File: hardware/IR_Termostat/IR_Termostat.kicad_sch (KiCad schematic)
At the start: 42 parts, among them J1 USB_C_Receptacle_PowerOnly_6P, J2 JST-PH-2mm, J3 Conn_01x03_Pin, Q1 PMOS, SW1 SW_Push_Dual, U1 TP4056-42-ESOP8, U2 XC6206P-3.3V, U4 MLX90614ESF-BAA-000-TU, U5 CH32V003JxMx, U6 DM-OLED096-636

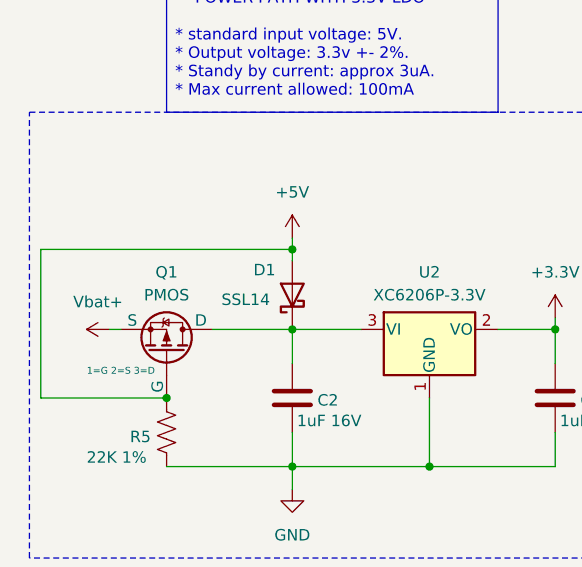
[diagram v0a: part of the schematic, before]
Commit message: Fix: power path mosfet footprint
 The footprint of the power path mosfet now it's pin-to-pin with the skemathic.
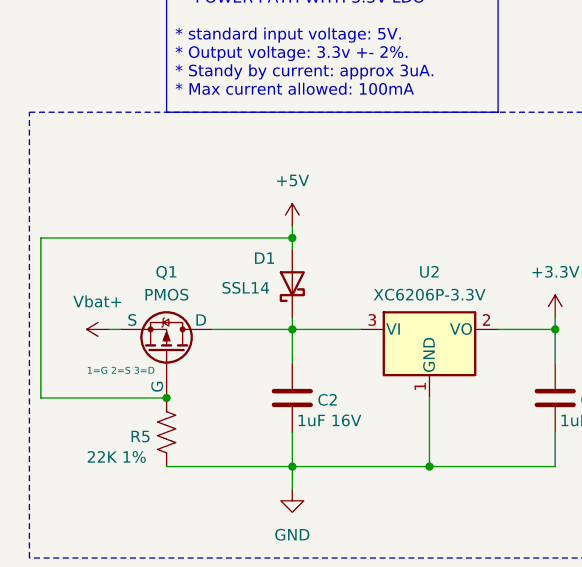
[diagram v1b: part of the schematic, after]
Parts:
- U4: footprint MLX90614ESF-BAA-000-TU:TO254P942H425-4 -> Library:TO254P942H425-4
- U6: footprint DM-OLED096-636:MODULE_DM-OLED096-636 -> Library:MODULE_DM-OLED096-636
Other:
- moved on the sheet: D1
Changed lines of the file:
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@@
 	)
 	(junction
+		(at 44.45 120.65)
+		(diameter 0)
+		(color 0 0 0 0)
+	)
+	(junction
 		(at 134.62 53.34)
 		(diameter 0)
@@
 	)
 	(junction
-		(at 44.45 121.92)
-		(diameter 0)
-		(color 0 0 0 0)
-	)
-	(junction
 		(at 148.59 53.34)
 		(diameter 0)
@@
 	(wire
 		(pts
-			(xy 44.45 120.65) (xy 44.45 121.92)
+			(xy 44.45 119.38) (xy 44.45 120.65)
 		)
 		(stroke
@@
 	(wire
 		(pts
-			(xy 16.51 121.92) (xy 16.51 138.43)
+			(xy 16.51 120.65) (xy 16.51 138.43)
 		)
 		(stroke
@@
 	(wire
 		(pts
+			(xy 44.45 129.54) (xy 44.45 130.81)
+		)
+		(stroke
+			(width 0)
+			(type default)
+		)
+	)
+	(wire
+		(pts
 			(xy 165.1 62.6446) (xy 165.1 69.85)
 		)
@@
 	(wire
 		(pts
-			(xy 44.45 121.92) (xy 44.45 123.19)
-		)
-		(stroke
-			(width 0)
-			(type default)
-		)
-	)
-	(wire
-		(pts
 			(xy 173.99 55.88) (xy 173.99 58.42)
 		)
@@
 	(wire
 		(pts
-			(xy 16.51 121.92) (xy 44.45 121.92)
+			(xy 16.51 120.65) (xy 44.45 120.65)
 		)
 		(stroke
@@
 	(wire
 		(pts
+			(xy 44.45 120.65) (xy 44.45 121.92)
+		)
+		(stroke
+			(width 0)
+			(type default)
+		)
+	)
+	(wire
+		(pts
 			(xy 118.11 184.15) (xy 133.35 184.15)
 		)
@@
 			)
 		)
-		(property "Footprint" "MLX90614ESF-BAA-000-TU:TO254P942H425-4"
+		(property "Footprint" "Library:TO254P942H425-4"
 			(at 267.208 112.268 0)
 			(effects
@@
 	(symbol
 		(lib_id "Diode:SS14")
-		(at 44.45 127 90)
+		(at 44.45 125.73 90)
 		(unit 1)
 		(exclude_from_sim no)
@@
 		(dnp no)
 		(property "Reference" "D1"
-			(at 40.132 124.206 90)
+			(at 40.132 122.936 90)
 			(effects
 				(font
@@
 		)
 		(property "Value" "SSL14"
-			(at 36.576 127.508 90)
+			(at 36.576 126.238 90)
 			(effects
 				(font
@@
 		)
 		(property "Footprint" "Diode_SMD:D_SMA_Handsoldering"
-			(at 48.895 127 0)
+			(at 48.895 125.73 0)
 			(effects
 				(font
@@
 		)
 		(property "Datasheet" "https://www.vishay.com/docs/88746/ss12.pdf"
-			(at 44.45 127 0)
+			(at 44.45 125.73 0)
 			(effects
 				(font
@@
 		)
 		(property "Description" "40V 1A Schottky Diode, SMA"
-			(at 44.45 127 0)
+			(at 44.45 125.73 0)
 			(effects
 				(font
@@
 			)
 		)
-		(property "Footprint" "DM-OLED096-636:MODULE_DM-OLED096-636"
+		(property "Footprint" "Library:MODULE_DM-OLED096-636"
 			(at 265.43 146.05 0)
 			(effects
@@
 	(symbol
 		(lib_id "power:+5V")
-		(at 44.45 120.65 0)
+		(at 44.45 119.38 0)
 		(unit 1)
 		(exclude_from_sim no)
@@
 		(fields_autoplaced yes)
 		(property "Reference" "#PWR06"
-			(at 44.45 124.46 0)
+			(at 44.45 123.19 0)
 			(effects
 				(font
@@
 		)
 		(property "Value" "+5V"
-			(at 44.45 115.57 0)
+			(at 44.45 114.3 0)
 			(effects
 				(font
@@
 		)
 		(property "Footprint" ""
-			(at 44.45 120.65 0)
+			(at 44.45 119.38 0)
 			(effects
 				(font
@@
 		)
 		(property "Datasheet" ""
-			(at 44.45 120.65 0)
+			(at 44.45 119.38 0)
 			(effects
 				(font
@@
 		)
 		(property "Description" "Power symbol creates a global label with name \"+5V\""
-			(at 44.45 120.65 0)
+			(at 44.45 119.38 0)
 			(effects
 				(font
